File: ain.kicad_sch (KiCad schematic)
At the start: 63 parts, among them J201 ANALOG_IN1, J202 ANALOG_IN2, J203 ANALOG_IN3, U201 OPA4134UA, U202 OPA2134

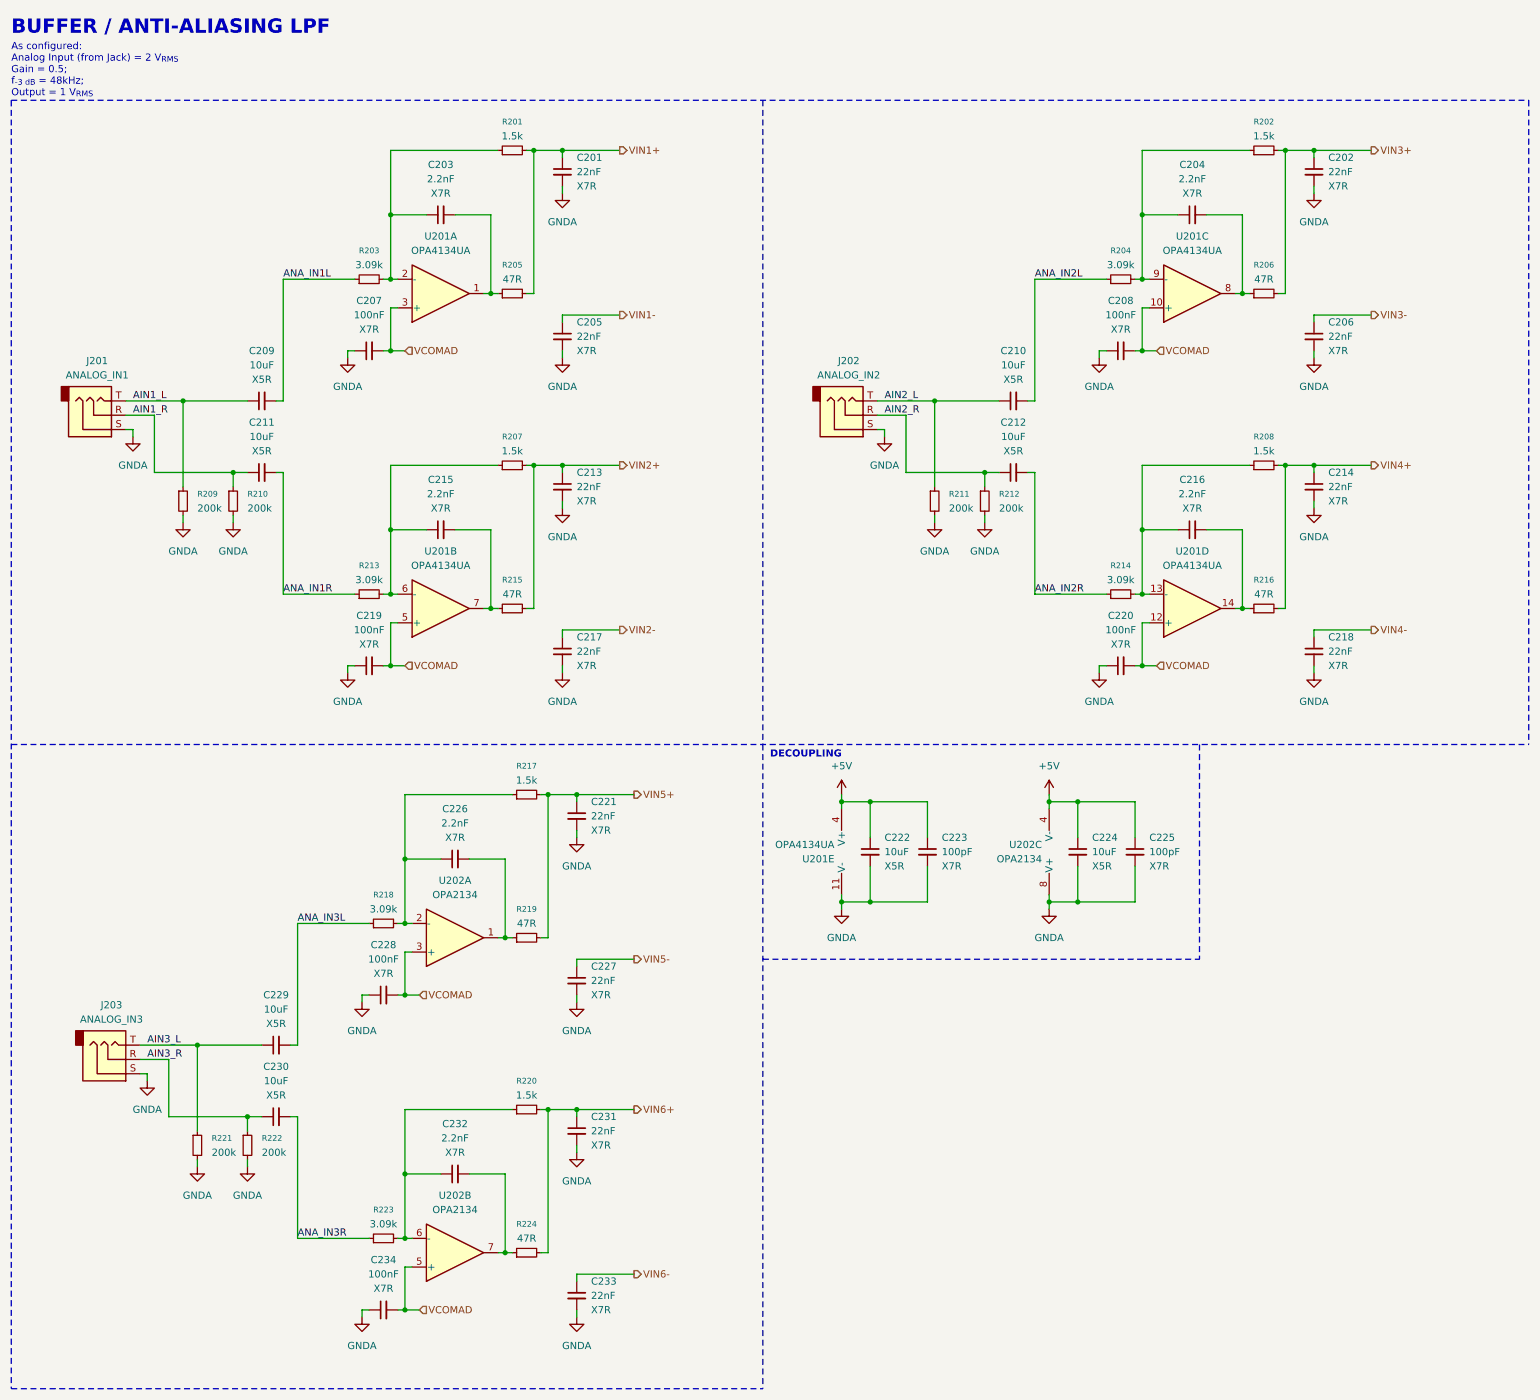
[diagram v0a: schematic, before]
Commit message: Cleaned up schematic
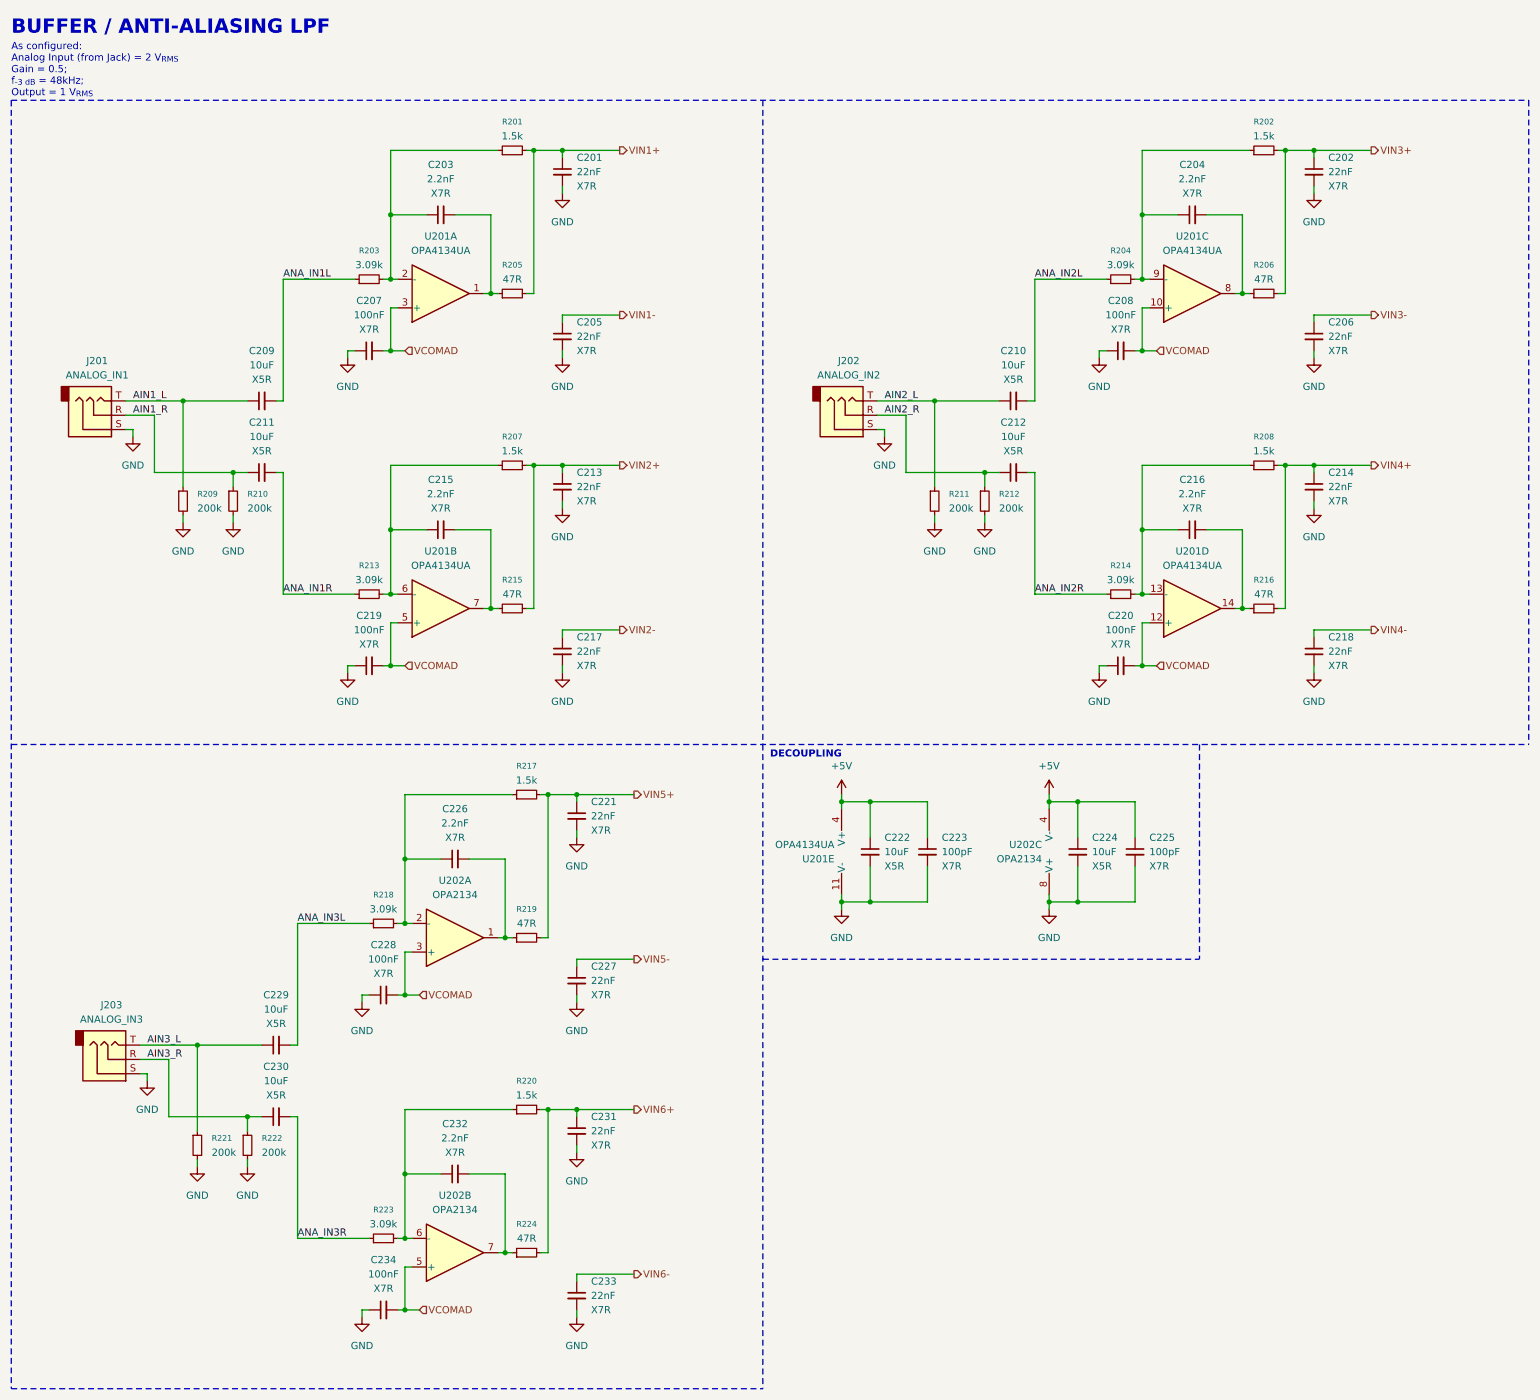
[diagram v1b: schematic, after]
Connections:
- net GNDA renamed GND
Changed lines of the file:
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@@
 			)
 		)
-		(property "Value" "GNDA"
+		(property "Value" "GND"
 			(at 177.8 200.66 0)
 			(effects
@@
 			)
 		)
-		(property "Value" "GNDA"
+		(property "Value" "GND"
 			(at 261.62 184.15 0)
 			(effects
@@
 			)
 		)
-		(property "Value" "GNDA"
+		(property "Value" "GND"
 			(at 177.8 256.54 0)
 			(effects
@@
 			)
 		)
-		(property "Value" "GNDA"
+		(property "Value" "GND"
 			(at 110.49 229.87 0)
 			(effects
@@
 			)
 		)
-		(property "Value" "GNDA"
+		(property "Value" "GND"
 			(at 137.16 86.36 0)
 			(effects
@@
 			)
 		)
-		(property "Value" "GNDA"
+		(property "Value" "GND"
 			(at 175.26 57.15 0)
 			(effects
@@
 			)
 		)
-		(property "Value" "GNDA"
+		(property "Value" "GND"
 			(at 232.41 100.33 0)
 			(effects
@@
 			)
 		)
-		(property "Value" "GNDA"
+		(property "Value" "GND"
 			(at 116.84 115.57 0)
 			(effects
@@
 			)
 		)
-		(property "Value" "GNDA"
+		(property "Value" "GND"
 			(at 250.19 115.57 0)
 			(effects
@@
 			)
 		)
-		(property "Value" "GNDA"
+		(property "Value" "GND"
 			(at 270.51 86.36 0)
 			(effects
@@
 			)
 		)
-		(property "Value" "GNDA"
+		(property "Value" "GND"
 			(at 107.95 115.57 0)
 			(effects
@@
 			)
 		)
-		(property "Value" "GNDA"
+		(property "Value" "GND"
 			(at 224.79 184.15 0)
 			(effects
@@
 			)
 		)
-		(property "Value" "GNDA"
+		(property "Value" "GND"
 			(at 308.61 142.24 0)
 			(effects
@@
 			)
 		)
-		(property "Value" "GNDA"
+		(property "Value" "GND"
 			(at 119.38 229.87 0)
 			(effects
@@
 			)
 		)
-		(property "Value" "GNDA"
+		(property "Value" "GND"
 			(at 308.61 86.36 0)
 			(effects
@@
 			)
 		)
-		(property "Value" "GNDA"
+		(property "Value" "GND"
 			(at 241.3 115.57 0)
 			(effects
@@
 			)
 		)
-		(property "Value" "GNDA"
+		(property "Value" "GND"
 			(at 270.51 142.24 0)
 			(effects
@@
 			)
 		)
-		(property "Value" "GNDA"
+		(property "Value" "GND"
 			(at 308.61 57.15 0)
 			(effects
@@
 			)
 		)
-		(property "Value" "GNDA"
+		(property "Value" "GND"
 			(at 308.61 113.03 0)
 			(effects
@@
 			)
 		)
-		(property "Value" "GNDA"
+		(property "Value" "GND"
 			(at 137.16 142.24 0)
 			(effects
@@
 			)
 		)
-		(property "Value" "GNDA"
+		(property "Value" "GND"
 			(at 175.26 113.03 0)
 			(effects
@@
 			)
 		)
-		(property "Value" "GNDA"
+		(property "Value" "GND"
 			(at 99.06 100.33 0)
 			(effects
@@
 			)
 		)
-		(property "Value" "GNDA"
+		(property "Value" "GND"
 			(at 177.8 171.45 0)
 			(effects
@@
 			)
 		)
-		(property "Value" "GNDA"
+		(property "Value" "GND"
 			(at 139.7 256.54 0)
 			(effects
@@
 			)
 		)
-		(property "Value" "GNDA"
+		(property "Value" "GND"
 			(at 101.6 214.63 0)
 			(effects
@@
 			)
 		)
-		(property "Value" "GNDA"
+		(property "Value" "GND"
 			(at 175.26 86.36 0)
 			(effects
@@
 			)
 		)
-		(property "Value" "GNDA"
+		(property "Value" "GND"
 			(at 139.7 200.66 0)
 			(effects
@@
 			)
 		)
-		(property "Value" "GNDA"
+		(property "Value" "GND"
 			(at 177.8 227.33 0)
 			(effects
@@
 			)
 		)
-		(property "Value" "GNDA"
+		(property "Value" "GND"
 			(at 175.26 142.24 0)
 			(effects

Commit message: finished routin, updated schematic, added PDF
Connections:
- net at C216.1, R208.1, R214.2: now also U201.9 (-); no longer U201.13 (-)
- net at C232.2, R224.1: now also U202.1; no longer U202.7
- net at C226.2, R219.1: now also U202.7; no longer U202.1
- net at C226.1, R217.1, R218.2: now also U202.6 (-); no longer U202.2 (-)
- net at C232.1, R220.1, R223.2: now also U202.2 (-); no longer U202.6 (-)
- net at C216.2, R216.1: now also U201.8; no longer U201.14
- net at C204.2, R206.1: now also U201.14; no longer U201.8
- net at C204.1, R202.1, R204.2: now also U201.13 (-); no longer U201.9 (-)
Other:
- moved on the sheet: U201C, U201D, U202A, U202B
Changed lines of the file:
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@@
 	(symbol
 		(lib_id "Amplifier_Operational:OPA2134")
-		(at 156.21 184.15 0)
+		(at 156.21 240.03 0)
 		(mirror x)
 		(unit 1)
@@
 		(fields_autoplaced yes)
 		(property "Reference" "U202"
-			(at 156.21 173.99 0)
+			(at 156.21 229.87 0)
 			(effects
 				(font
@@
 		)
 		(property "Value" "OPA2134"
-			(at 156.21 176.53 0)
+			(at 156.21 232.41 0)
 			(effects
 				(font
@@
 		)
 		(property "Footprint" "Package_SO:SOIC-8_3.9x4.9mm_P1.27mm"
-			(at 156.21 184.15 0)
+			(at 156.21 240.03 0)
 			(effects
 				(font
@@
 		)
 		(property "Datasheet" "http://www.ti.com/lit/ds/symlink/opa134.pdf"
-			(at 156.21 184.15 0)
+			(at 156.21 240.03 0)
 			(effects
 				(font
@@
 		)
 		(property "Description" "Dual SoundPlus High Performance Audio Operational Amplifiers, DIP-8/SOIC-8"
-			(at 156.21 184.15 0)
+			(at 156.21 240.03 0)
 			(effects
 				(font
@@
 	(symbol
 		(lib_id "Amplifier_Operational:OPA2134")
-		(at 156.21 240.03 0)
+		(at 156.21 184.15 0)
 		(mirror x)
 		(unit 2)
@@
 		(fields_autoplaced yes)
 		(property "Reference" "U202"
-			(at 156.21 229.87 0)
+			(at 156.21 173.99 0)
 			(effects
 				(font
@@
 		)
 		(property "Value" "OPA2134"
-			(at 156.21 232.41 0)
+			(at 156.21 176.53 0)
 			(effects
 				(font
@@
 		)
 		(property "Footprint" "Package_SO:SOIC-8_3.9x4.9mm_P1.27mm"
-			(at 156.21 240.03 0)
+			(at 156.21 184.15 0)
 			(effects
 				(font
@@
 		)
 		(property "Datasheet" "http://www.ti.com/lit/ds/symlink/opa134.pdf"
-			(at 156.21 240.03 0)
+			(at 156.21 184.15 0)
 			(effects
 				(font
@@
 		)
 		(property "Description" "Dual SoundPlus High Performance Audio Operational Amplifiers, DIP-8/SOIC-8"
-			(at 156.21 240.03 0)
+			(at 156.21 184.15 0)
 			(effects
 				(font
@@
 	(symbol
 		(lib_id "Amplifier_Operational:OPA4134")
-		(at 287.02 125.73 0)
+		(at 287.02 69.85 0)
 		(mirror x)
 		(unit 4)
@@
 		(fields_autoplaced yes)
 		(property "Reference" "U201"
-			(at 287.02 115.57 0)
+			(at 287.02 59.69 0)
 			(effects
 				(font
@@
 		)
 		(property "Value" "OPA4134UA"
-			(at 287.02 118.11 0)
+			(at 287.02 62.23 0)
 			(effects
 				(font
@@
 		)
 		(property "Footprint" "Package_SO:SOIC-14_3.9x8.7mm_P1.27mm"
-			(at 285.75 128.27 0)
+			(at 285.75 72.39 0)
 			(effects
 				(font
@@
 		)
 		(property "Datasheet" "http://www.ti.com/lit/ds/symlink/opa134.pdf"
-			(at 288.29 130.81 0)
+			(at 288.29 74.93 0)
 			(effects
 				(font
@@
 		)
 		(property "Description" "Quad SoundPlus High Performance Audio Operational Amplifiers, SOIC-14"
-			(at 287.02 125.73 0)
+			(at 287.02 69.85 0)
 			(effects
 				(font
@@
 	(symbol
 		(lib_id "Amplifier_Operational:OPA4134")
-		(at 287.02 69.85 0)
+		(at 287.02 125.73 0)
 		(mirror x)
 		(unit 3)
@@
 		(fields_autoplaced yes)
 		(property "Reference" "U201"
-			(at 287.02 59.69 0)
+			(at 287.02 115.57 0)
 			(effects
 				(font
@@
 		)
 		(property "Value" "OPA4134UA"
-			(at 287.02 62.23 0)
+			(at 287.02 118.11 0)
 			(effects
 				(font
@@
 		)
 		(property "Footprint" "Package_SO:SOIC-14_3.9x8.7mm_P1.27mm"
-			(at 285.75 72.39 0)
+			(at 285.75 128.27 0)
 			(effects
 				(font
@@
 		)
 		(property "Datasheet" "http://www.ti.com/lit/ds/symlink/opa134.pdf"
-			(at 288.29 74.93 0)
+			(at 288.29 130.81 0)
 			(effects
 				(font
@@
 		)
 		(property "Description" "Quad SoundPlus High Performance Audio Operational Amplifiers, SOIC-14"
-			(at 287.02 69.85 0)
+			(at 287.02 125.73 0)
 			(effects
 				(font
